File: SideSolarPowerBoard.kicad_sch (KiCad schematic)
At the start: 19 parts, among them U1 SPV1040

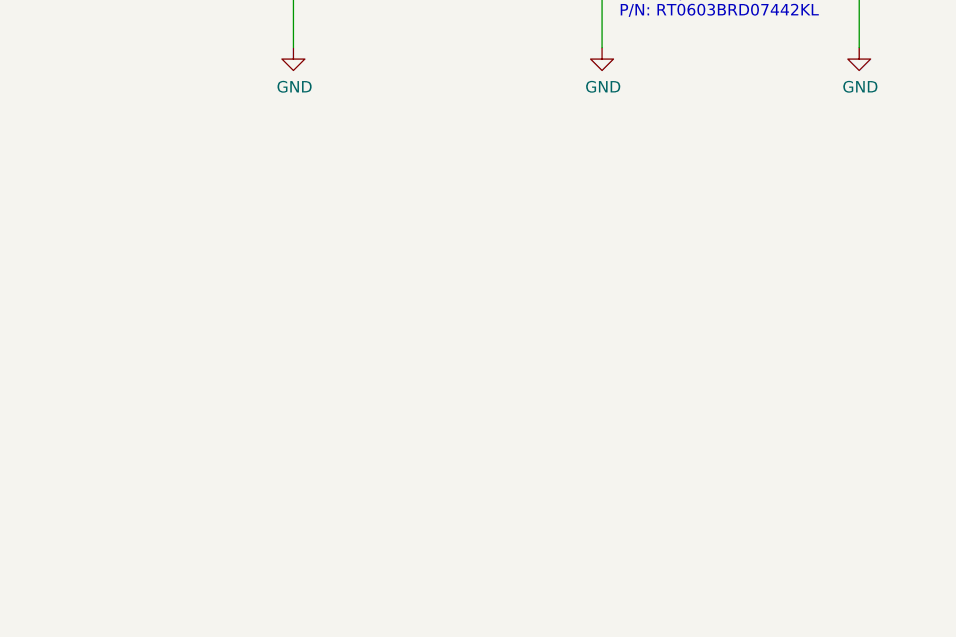
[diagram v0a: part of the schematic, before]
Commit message: Quickly add a sensor and a connector
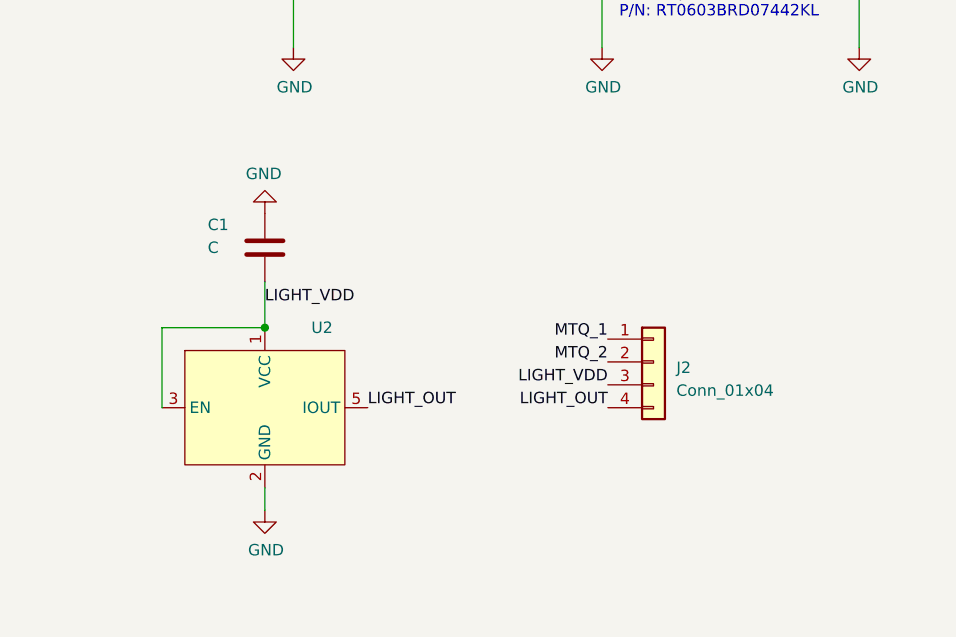
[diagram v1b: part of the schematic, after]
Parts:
- added C1: C, Capacitor_SMD:C_0402_1005Metric_Pad0.74x0.62mm_HandSolder, symbol Device:C
- added J2: Conn_01x04, Connector_Molex:Molex_PicoBlade_53398-0471_1x04-1MP_P1.25mm_Vertical, symbol Connector_Generic:Conn_01x04
- added U2: ~, POQUITO_Panel_Library:WSOF-5, symbol POQUITO_Panel_Library:BH1682FVC
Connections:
- net GND: now also C1.2, U2.2 (GND)
- new net LIGHT_OUT: J2.4 (Pin_4), U2.5 (IOUT)
- new net LIGHT_VDD: C1.1, J2.3 (Pin_3), U2.1 (VCC), U2.3 (EN)
- new net MTQ_1: J2.1 (Pin_1)
- new net MTQ_2: J2.2 (Pin_2)
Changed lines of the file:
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@@
   (junction (at 102.87 116.84) (diameter 0) (color 0 0 0 0)
   )
+  (junction (at 156.21 121.92) (diameter 0) (color 0 0 0 0)
+  )
   (wire (pts (xy 153.035 69.215) (xy 151.765 69.215))
     (stroke (width 0) (type default))
@@
     (stroke (width 0) (type default))
   )
+  (wire (pts (xy 144.78 121.92) (xy 156.21 121.92))
+    (stroke (width 0) (type default))
+  )
   (wire (pts (xy 231.14 57.785) (xy 222.25 57.785))
     (stroke (width 0) (type default))
@@
     (stroke (width 0) (type default))
   )
+  (wire (pts (xy 144.78 130.81) (xy 144.78 121.92))
+    (stroke (width 0) (type default))
+  )
   (wire (pts (xy 158.115 69.215) (xy 161.925 69.215))
     (stroke (width 0) (type default))
@@
     (stroke (width 0) (type default))
   )
+  (wire (pts (xy 156.21 116.84) (xy 156.21 121.92))
+    (stroke (width 0) (type default))
+  )
   (wire (pts (xy 178.435 61.595) (xy 178.435 57.785))
     (stroke (width 0) (type default))
@@
   )
   (wire (pts (xy 139.065 78.105) (xy 139.065 76.835))
+    (stroke (width 0) (type default))
+  )
+  (wire (pts (xy 156.21 139.7) (xy 156.21 142.24))
     (stroke (width 0) (type default))
   )
@@
     (effects (font (size 1.27 1.27)) (justify left bottom))
   )
+  (label "LIGHT_VDD" (at 194.31 128.27 180) (fields_autoplaced)
+    (effects (font (size 1.27 1.27)) (justify right bottom))
+  )
+  (label "LIGHT_OUT" (at 167.64 130.81 0) (fields_autoplaced)
+    (effects (font (size 1.27 1.27)) (justify left bottom))
+  )
+  (label "LIGHT_OUT" (at 194.31 130.81 180) (fields_autoplaced)
+    (effects (font (size 1.27 1.27)) (justify right bottom))
+  )
   (label "VCTRL" (at 151.765 69.215 0)
     (effects (font (size 1.27 1.27)) (justify left bottom))
@@
     (effects (font (size 1.27 1.27)) (justify right bottom))
   )
+  (label "LIGHT_VDD" (at 156.21 119.38 0) (fields_autoplaced)
+    (effects (font (size 1.27 1.27)) (justify left bottom))
+  )
+  (label "MTQ_1" (at 194.31 123.19 180) (fields_autoplaced)
+    (effects (font (size 1.27 1.27)) (justify right bottom))
+  )
   (label "VOUT" (at 151.765 59.055 0)
     (effects (font (size 1.27 1.27)) (justify left bottom))
@@
   (label "PV-" (at 110.49 130.81 0)
     (effects (font (size 1.27 1.27)) (justify left bottom))
+  )
+  (label "MTQ_2" (at 194.31 125.73 180) (fields_autoplaced)
+    (effects (font (size 1.27 1.27)) (justify right bottom))
   )
   (symbol (lib_id "SideSolarPowerBoard-rescue:INDUCTOR-pspice") (at 111.125 57.785 0) (unit 1)
@@
         )
       )
+    )
+  )
+  (symbol (lib_id "Device:C") (at 156.21 113.03 180) (unit 1)
+    (in_bom yes) (on_board yes) (dnp no)
+    (property "Reference" "C1" (at 149.86 110.49 0)
+      (effects (font (size 1.27 1.27)) (justify right))
+    )
+    (property "Value" "C" (at 149.86 113.03 0)
+      (effects (font (size 1.27 1.27)) (justify right))
+    )
+    (property "Footprint" "Capacitor_SMD:C_0402_1005Metric_Pad0.74x0.62mm_HandSolder" (at 155.2448 109.22 0)
+      (effects (font (size 1.27 1.27)) hide)
+    )
+    (property "Datasheet" "~" (at 156.21 113.03 0)
+      (effects (font (size 1.27 1.27)) hide)
+    )
+    (pin "1")
+    (pin "2")
+    (instances
+      (project "SideSolarPowerBoard"
+        (path "/4203ae70-d906-4629-a666-ed898b86e72f"
+          (reference "C1") (unit 1)
+        )
+      )
+    )
+  )
+  (symbol (lib_id "POQUITO_Panel_Library:BH1682FVC") (at 156.21 130.81 0) (unit 1)
+    (in_bom yes) (on_board yes) (dnp no)
+    (property "Reference" "U2" (at 162.56 121.92 0)
+      (effects (font (size 1.27 1.27)))
+    )
+    (property "Value" "~" (at 136.525 127.508 0)
+      (effects (font (size 1.27 1.27)))
+    )
+    (property "Footprint" "POQUITO_Panel_Library:WSOF-5" (at 136.525 127.508 0)
+      (effects (font (size 1.27 1.27)) hide)
+    )
+    (property "Datasheet" "https://fscdn.rohm.com/en/products/databook/datasheet/ic/sensor/light/bh1682fvc-e.pdf" (at 136.525 127.508 0)
+      (effects (font (size 1.27 1.27)) hide)
+    )
+    (pin "1")
+    (pin "2")
+    (pin "3")
+    (pin "4")
+    (pin "5")
+    (instances
+      (project "SideSolarPowerBoard"
+        (path "/4203ae70-d906-4629-a666-ed898b86e72f"
+          (reference "U2") (unit 1)
+        )
+      )
+    )
+  )
+  (symbol (lib_id "power:GND") (at 156.21 142.24 0) (unit 1)
+    (in_bom yes) (on_board yes) (dnp no)
+    (property "Reference" "#PWR02" (at 156.21 148.59 0)
+      (effects (font (size 1.27 1.27)) hide)
+    )
+    (property "Value" "GND" (at 156.337 146.6342 0)
+      (effects (font (size 1.27 1.27)))
+    )
+    (property "Footprint" "" (at 156.21 142.24 0)
+      (effects (font (size 1.27 1.27)) hide)
+    )
+    (property "Datasheet" "" (at 156.21 142.24 0)
+      (effects (font (size 1.27 1.27)) hide)
+    )
+    (pin "1")
+    (instances
+      (project "SideSolarPowerBoard"
+        (path "/4203ae70-d906-4629-a666-ed898b86e72f"
+          (reference "#PWR02") (unit 1)
+        )
+      )
+    )
+  )
+  (symbol (lib_id "Connector_Generic:Conn_01x04") (at 199.39 125.73 0) (unit 1)
+    (in_bom yes) (on_board yes) (dnp no) (fields_autoplaced)
+    (property "Reference" "J2" (at 201.93 126.365 0)
+      (effects (font (size 1.27 1.27)) (justify left))
+    )
+    (property "Value" "Conn_01x04" (at 201.93 128.905 0)
+      (effects (font (size 1.27 1.27)) (justify left))
+    )
+    (property "Footprint" "Connector_Molex:Molex_PicoBlade_53398-0471_1x04-1MP_P1.25mm_Vertical" (at 199.39 125.73 0)
+      (effects (font (size 1.27 1.27)) hide)
+    )
+    (property "Datasheet" "~" (at 199.39 125.73 0)
+      (effects (font (size 1.27 1.27)) hide)
+    )
+    (pin "1")
+    (pin "2")
+    (pin "3")
+    (pin "4")
+    (instances
+      (project "SideSolarPowerBoard"
+        (path "/4203ae70-d906-4629-a666-ed898b86e72f"
+          (reference "J2") (unit 1)
+        )
+      )
+    )
+  )
+  (symbol (lib_id "power:GND") (at 156.21 109.22 180) (unit 1)
+    (in_bom yes) (on_board yes) (dnp no)
+    (property "Reference" "#PWR03" (at 156.21 102.87 0)
+      (effects (font (size 1.27 1.27)) hide)
+    )
+    (property "Value" "GND" (at 156.083 104.8258 0)
+      (effects (font (size 1.27 1.27)))
+    )
+    (property "Footprint" "" (at 156.21 109.22 0)
+      (effects (font (size 1.27 1.27)) hide)
+    )
+    (property "Datasheet" "" (at 156.21 109.22 0)
+      (effects (font (size 1.27 1.27)) hide)
+    )
+    (pin "1")
+    (instances
+      (project "SideSolarPowerBoard"
+        (path "/4203ae70-d906-4629-a666-ed898b86e72f"
+          (reference "#PWR03") (unit 1)
+        )
+      )

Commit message: Update to pogo pin ADCS design
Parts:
- C1: value C -> 100nF; MPN (none) -> C0402C104K8RACTU
- D_OUT1: MPN SMM4F5.0A-TR -> SMM4F5.0A-TR
- J2: MPN (none) -> 53398-0471
- U2: value ~ -> BH1682FVC; MPN (none) -> BH1682FVC-TR
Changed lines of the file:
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@@
   (title_block
     (title "Side Solar Power Board")
-    (date "2019-11-19")
-    (comment 1 "CERN Open Hardware Licence v1.2 ")
+    (date "2023-09-11")
+    (rev "2")
+    (comment 1 "CERN Open Hardware Licence Version 2 - Weakly Reciprocal")
   )
   (junction (at 102.87 130.81) (diameter 0) (color 0 0 0 0)
@@
     (effects (font (size 1.27 1.27)) (justify left bottom))
   )
-  (label "PV+" (at 64.135 57.785 0)
+  (label "PV+" (at 64.135 57.785 0) (fields_autoplaced)
     (effects (font (size 1.27 1.27)) (justify left bottom))
   )
-  (label "ICTRL-" (at 151.765 66.675 0)
+  (label "ICTRL-" (at 151.765 66.675 0) (fields_autoplaced)
     (effects (font (size 1.27 1.27)) (justify left bottom))
   )
-  (label "XSHUT" (at 126.365 64.135 180)
+  (label "XSHUT" (at 126.365 64.135 180) (fields_autoplaced)
     (effects (font (size 1.27 1.27)) (justify right bottom))
   )
-  (label "ICTRL+" (at 151.765 61.595 0)
+  (label "ICTRL+" (at 151.765 61.595 0) (fields_autoplaced)
     (effects (font (size 1.27 1.27)) (justify left bottom))
   )
@@
     (effects (font (size 1.27 1.27)) (justify right bottom))
   )
-  (label "VCTRL" (at 151.765 69.215 0)
+  (label "VCTRL" (at 151.765 69.215 0) (fields_autoplaced)
     (effects (font (size 1.27 1.27)) (justify left bottom))
   )
-  (label "LX" (at 126.365 61.595 180)
+  (label "LX" (at 126.365 61.595 180) (fields_autoplaced)
     (effects (font (size 1.27 1.27)) (justify right bottom))
   )
-  (label "MPP-SET" (at 126.365 66.675 180)
+  (label "MPP-SET" (at 126.365 66.675 180) (fields_autoplaced)
     (effects (font (size 1.27 1.27)) (justify right bottom))
   )
@@
     (effects (font (size 1.27 1.27)) (justify right bottom))
   )
-  (label "VOUT" (at 151.765 59.055 0)
+  (label "VOUT" (at 151.765 59.055 0) (fields_autoplaced)
     (effects (font (size 1.27 1.27)) (justify left bottom))
   )
-  (label "PV+" (at 110.49 116.84 0)
+  (label "PV+" (at 110.49 116.84 0) (fields_autoplaced)
     (effects (font (size 1.27 1.27)) (justify left bottom))
   )
-  (label "VBAT+" (at 231.14 57.785 180)
+  (label "VBAT+" (at 231.14 57.785 180) (fields_autoplaced)
     (effects (font (size 1.27 1.27)) (justify right bottom))
   )
-  (label "PV-" (at 110.49 130.81 0)
+  (label "PV-" (at 110.49 130.81 0) (fields_autoplaced)
     (effects (font (size 1.27 1.27)) (justify left bottom))
   )
@@
       (effects (font (size 1.27 1.27)) hide)
     )
-    (property "MPN" " SMM4F5.0A-TR " (at 222.25 73.025 0)
+    (property "MPN" "SMM4F5.0A-TR " (at 222.25 73.025 0)
       (effects (font (size 1.27 1.27)) hide)
     )
@@
   )
   (symbol (lib_id "Device:C") (at 156.21 113.03 180) (unit 1)
-    (in_bom yes) (on_board yes) (dnp no)
-    (property "Reference" "C1" (at 149.86 110.49 0)
+    (in_bom yes) (on_board yes) (dnp no) (fields_autoplaced)
+    (property "Reference" "C1" (at 160.02 112.395 0)
       (effects (font (size 1.27 1.27)) (justify right))
     )
-    (property "Value" "C" (at 149.86 113.03 0)
+    (property "Value" "100nF" (at 160.02 114.935 0)
       (effects (font (size 1.27 1.27)) (justify right))
     )
@@
       (effects (font (size 1.27 1.27)) hide)
     )
+    (property "MPN" "C0402C104K8RACTU" (at 156.21 113.03 0)
+      (effects (font (size 1.27 1.27)) hide)
+    )
     (pin "1")
     (pin "2")
@@
       (effects (font (size 1.27 1.27)))
     )
-    (property "Value" "~" (at 136.525 127.508 0)
+    (property "Value" "BH1682FVC" (at 136.525 127.508 0)
       (effects (font (size 1.27 1.27)))
     )
@@
     )
     (property "Datasheet" "https://fscdn.rohm.com/en/products/databook/datasheet/ic/sensor/light/bh1682fvc-e.pdf" (at 136.525 127.508 0)
+      (effects (font (size 1.27 1.27)) hide)
+    )
+    (property "MPN" "BH1682FVC-TR" (at 156.21 130.81 0)
       (effects (font (size 1.27 1.27)) hide)
     )
@@
       (effects (font (size 1.27 1.27)) hide)
     )
+    (property "MPN" "53398-0471" (at 199.39 125.73 0)
+      (effects (font (size 1.27 1.27)) hide)
+    )

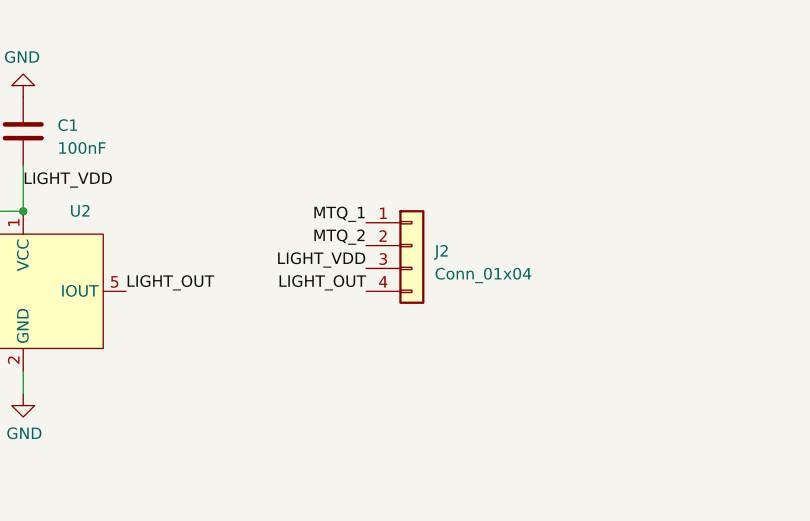
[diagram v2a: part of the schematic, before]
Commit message: Fix position of Lx
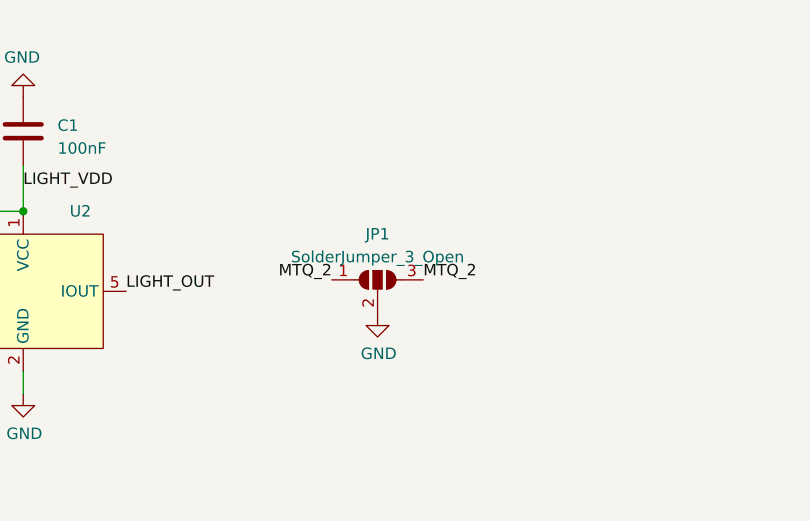
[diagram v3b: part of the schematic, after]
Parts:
- removed J2: Conn_01x04, Connector_Molex:Molex_PicoBlade_53398-0471_1x04-1MP_P1.25mm_Vertical, symbol Connector_Generic:Conn_01x04
- added JP1: SolderJumper_3_Open, Jumper:SolderJumper-3_P1.3mm_Open_RoundedPad1.0x1.5mm_NumberLabels, symbol Jumper:SolderJumper_3_Open
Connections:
- net GND: now also JP1.2 (C)
- net MTQ_2: now also JP1.1 (A), JP1.3 (B)
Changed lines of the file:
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@@
     (effects (font (size 1.27 1.27)) (justify left bottom))
   )
-  (label "LIGHT_VDD" (at 194.31 128.27 180) (fields_autoplaced)
+  (label "MTQ_2" (at 190.5 129.54 180) (fields_autoplaced)
     (effects (font (size 1.27 1.27)) (justify right bottom))
   )
@@
     (effects (font (size 1.27 1.27)) (justify left bottom))
   )
-  (label "LIGHT_OUT" (at 194.31 130.81 180) (fields_autoplaced)
-    (effects (font (size 1.27 1.27)) (justify right bottom))
-  )
   (label "VCTRL" (at 151.765 69.215 0) (fields_autoplaced)
     (effects (font (size 1.27 1.27)) (justify left bottom))
@@
     (effects (font (size 1.27 1.27)) (justify left bottom))
   )
-  (label "MTQ_1" (at 194.31 123.19 180) (fields_autoplaced)
-    (effects (font (size 1.27 1.27)) (justify right bottom))
-  )
   (label "VOUT" (at 151.765 59.055 0) (fields_autoplaced)
     (effects (font (size 1.27 1.27)) (justify left bottom))
   )
+  (label "MTQ_2" (at 200.66 129.54 0) (fields_autoplaced)
+    (effects (font (size 1.27 1.27)) (justify left bottom))
+  )
   (label "PV+" (at 110.49 116.84 0) (fields_autoplaced)
     (effects (font (size 1.27 1.27)) (justify left bottom))
@@
   (label "PV-" (at 110.49 130.81 0) (fields_autoplaced)
     (effects (font (size 1.27 1.27)) (justify left bottom))
-  )
-  (label "MTQ_2" (at 194.31 125.73 180) (fields_autoplaced)
-    (effects (font (size 1.27 1.27)) (justify right bottom))
   )
   (symbol (lib_id "SideSolarPowerBoard-rescue:INDUCTOR-pspice") (at 111.125 57.785 0) (unit 1)
@@
     )
   )
+  (symbol (lib_id "Jumper:SolderJumper_3_Open") (at 195.58 129.54 0) (unit 1)
+    (in_bom yes) (on_board yes) (dnp no) (fields_autoplaced)
+    (property "Reference" "JP1" (at 195.58 124.46 0)
+      (effects (font (size 1.27 1.27)))
+    )
+    (property "Value" "SolderJumper_3_Open" (at 195.58 127 0)
+      (effects (font (size 1.27 1.27)))
+    )
+    (property "Footprint" "Jumper:SolderJumper-3_P1.3mm_Open_RoundedPad1.0x1.5mm_NumberLabels" (at 195.58 129.54 0)
+      (effects (font (size 1.27 1.27)) hide)
+    )
+    (property "Datasheet" "~" (at 195.58 129.54 0)
+      (effects (font (size 1.27 1.27)) hide)
+    )
+    (pin "1")
+    (pin "2")
+    (pin "3")
+    (instances
+      (project "SideSolarPowerBoard"
+        (path "/4203ae70-d906-4629-a666-ed898b86e72f"
+          (reference "JP1") (unit 1)
+        )
+      )
+    )
+  )
+  (symbol (lib_id "power:GND") (at 195.58 133.35 0) (unit 1)
+    (in_bom yes) (on_board yes) (dnp no)
+    (property "Reference" "#PWR04" (at 195.58 139.7 0)
+      (effects (font (size 1.27 1.27)) hide)
+    )
+    (property "Value" "GND" (at 195.707 137.7442 0)
+      (effects (font (size 1.27 1.27)))
+    )
+    (property "Footprint" "" (at 195.58 133.35 0)
+      (effects (font (size 1.27 1.27)) hide)
+    )
+    (property "Datasheet" "" (at 195.58 133.35 0)
+      (effects (font (size 1.27 1.27)) hide)
+    )
+    (pin "1")
+    (instances
+      (project "SideSolarPowerBoard"
+        (path "/4203ae70-d906-4629-a666-ed898b86e72f"
+          (reference "#PWR04") (unit 1)
+        )
+      )
+    )
+  )
   (symbol (lib_id "Device:C") (at 156.21 113.03 180) (unit 1)
     (in_bom yes) (on_board yes) (dnp no) (fields_autoplaced)
@@
         )
       )
-    )
-  )
-  (symbol (lib_id "Connector_Generic:Conn_01x04") (at 199.39 125.73 0) (unit 1)
-    (in_bom yes) (on_board yes) (dnp no) (fields_autoplaced)
-    (property "Reference" "J2" (at 201.93 126.365 0)
-      (effects (font (size 1.27 1.27)) (justify left))
-    )
-    (property "Value" "Conn_01x04" (at 201.93 128.905 0)
-      (effects (font (size 1.27 1.27)) (justify left))
-    )
-    (property "Footprint" "Connector_Molex:Molex_PicoBlade_53398-0471_1x04-1MP_P1.25mm_Vertical" (at 199.39 125.73 0)
-      (effects (font (size 1.27 1.27)) hide)
-    )
-    (property "Datasheet" "~" (at 199.39 125.73 0)
-      (effects (font (size 1.27 1.27)) hide)
-    )
-    (property "MPN" "53398-0471" (at 199.39 125.73 0)
-      (effects (font (size 1.27 1.27)) hide)
-    )
-    (pin "1")
-    (pin "2")
-    (pin "3")
-    (pin "4")
-    (instances
-      (project "SideSolarPowerBoard"
-        (path "/4203ae70-d906-4629-a666-ed898b86e72f"
-          (reference "J2") (unit 1)
-        )
-      )
